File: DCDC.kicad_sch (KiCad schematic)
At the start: 25 parts, among them U5 LM76005RNPR

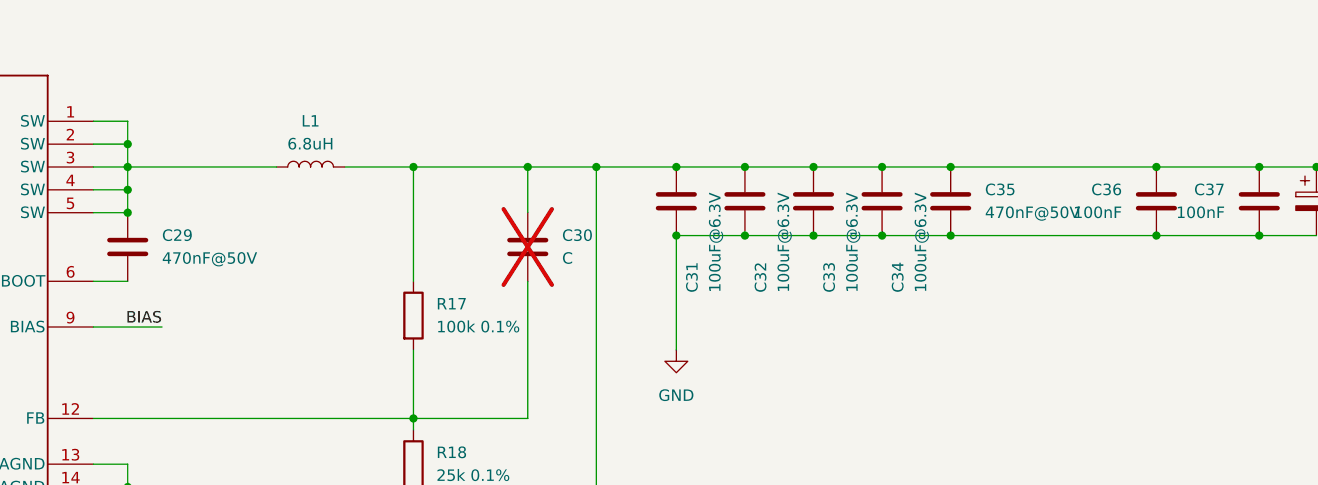
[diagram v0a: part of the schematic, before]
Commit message: BOM optimization
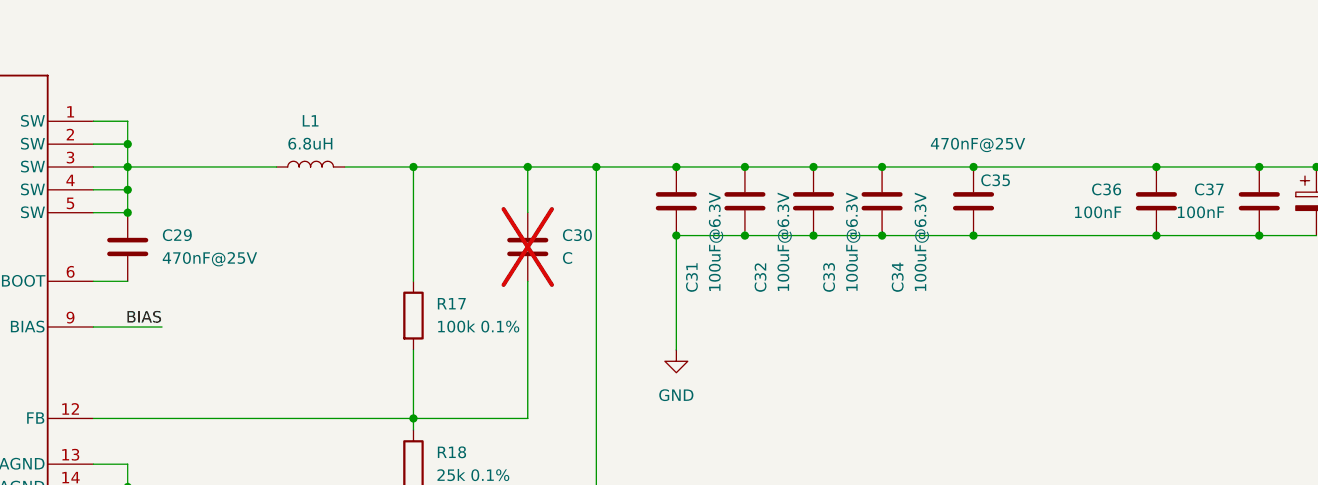
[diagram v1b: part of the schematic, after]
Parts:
- C29, C35: value 470nF@50V -> 470nF@25V; footprint Capacitor_SMD:C_0805_2012Metric -> Capacitor_SMD:C_0603_1608Metric; JLC C13967 -> C1623
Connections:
- net 5V: now also C35.2; no longer C35.1
- net GND: now also C35.1; no longer C35.2

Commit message: Prepare for next production - Slightly adapt part selection - Add TC2050 holes
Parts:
- C14: JLC C22387801 -> (none); LCSC Part # (none) -> C22387801
- C24, C25: JLC C13585 -> (none); LCSC Part # (none) -> C13585
- C26: JLC C13967 -> (none); LCSC Part # (none) -> C13967
- C28: JLC C377773 -> (none); LCSC Part # (none) -> C377773
- C29, C35: JLC C1623 -> (none); LCSC Part # (none) -> C1623
- C31, C32, C33, C34: JLC C15008 -> (none); LCSC Part # (none) -> C15008
- C36, C37: JLC C307331 -> (none); LCSC Part # (none) -> C307331
- C51: JLC C354368 -> (none); LCSC Part # (none) -> C354368
- D1: JLC C2297 -> (none); LCSC Part # (none) -> C2297
- L1: JLC C408485 -> (none); LCSC Part # (none) -> C408485
- R16: JLC C149504 -> (none); LCSC Part # (none) -> C149504
- R17: JLC C122537 -> (none); LCSC Part # (none) -> C122537
- R18: JLC C153306 -> (none); LCSC Part # (none) -> C153306
- R19: JLC C17513 -> (none); LCSC Part # (none) -> C17513
- R26: JLC C17477 -> (none); LCSC Part # (none) -> C17477
- U5: MFPN (none) -> LM76005RNPR; MP LM76005RNPR -> (none)

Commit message: Next proto prep
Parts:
- C51: LCSC Part # C354368 -> C28323
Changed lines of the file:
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@@
 			)
 		)
-		(property "Description" "Unpolarized capacitor"
+		(property "Description" "1uF 50V X7R ±10% 0805 Multilayer Ceramic Capacitors MLCC - SMD/SMT ROHS"
 			(at 346.71 170.18 0)
 			(effects
@@
 			)
 		)
-		(property "LCSC Part #" "C354368"
+		(property "LCSC Part #" "C28323"
 			(at 346.71 170.18 0)
 			(effects

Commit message: Production state
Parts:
- R19: value 1k -> 10k; footprint Resistor_SMD:R_0805_2012Metric -> Resistor_SMD:R_0402_1005Metric; LCSC Part # C17513 -> C25744
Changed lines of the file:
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@@
 	(title_block
 		(title "OpenMower SABO Carrierboard for Series I & II")
-		(date "2025-10-12")
+		(date "2026-04-04")
 		(rev "v0.4")
 		(company "Apeheanger <joerg@ebeling.ws> for OpenMower")
@@
 			)
 		)
-		(property "Value" "1k"
+		(property "Value" "10k"
 			(at 340.36 135.8899 0)
 			(effects
@@
 			)
 		)
-		(property "Footprint" "Resistor_SMD:R_0805_2012Metric"
+		(property "Footprint" "Resistor_SMD:R_0402_1005Metric"
 			(at 336.042 134.62 90)
 			(effects
@@
 			)
 		)
-		(property "Description" "Resistor"
+		(property "Description" "62.5mW Thick Film Resistors 50V ±100ppm/℃ ±1% 10kΩ 0402 Chip Resistor"
 			(at 337.82 134.62 0)
 			(effects
@@
 			)
 		)
-		(property "LCSC Part #" "C17513"
+		(property "LCSC Part #" "C25744"
 			(at 337.82 134.62 0)
 			(effects
